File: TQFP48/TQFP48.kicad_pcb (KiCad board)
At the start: 2 copper layers, 61.2 x 18 mm, 11 parts, among them J1 Conn_01x24, J2 Conn_02x24_Counter_Clockwise, J3 Conn_02x24_Counter_Clockwise, J4 Conn_01x24, J5 Conn_01x05

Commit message: Board Updates
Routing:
- net Net-(J2-Pad48): track 54.5 -> 62.1 mm
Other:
- board size 61.2 x 18 mm -> 61 x 17.8 mm
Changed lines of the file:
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@@
     (thickness 1.6)
     (drawings 76)
-    (tracks 326)
+    (tracks 327)
     (zones 0)
     (modules 11)
@@
     (38 B.Mask user hide)
     (39 F.Mask user hide)
-    (40 Dwgs.User user)
+    (40 Dwgs.User user hide)
     (41 Cmts.User user hide)
     (42 Eco1.User user hide)
@@
       (xy 0.500964 -3.601424)) (layer F.SilkS) (width 0.01))
   )
-  (dimension 18.034 (width 0.15) (layer Dwgs.User)
-    (gr_text "18.034 mm" (at 30.196 35.56 270) (layer Dwgs.User)
+  (gr_line (start 97.917 43.18) (end 97.917 27.94) (layer Edge.Cuts) (width 0.05))
+  (gr_line (start 38.227 44.45) (end 96.647 44.45) (layer Edge.Cuts) (width 0.05))
+  (gr_line (start 36.957 27.94) (end 36.957 43.18) (layer Edge.Cuts) (width 0.05))
+  (gr_line (start 96.647 26.67) (end 38.227 26.67) (layer Edge.Cuts) (width 0.05))
+  (gr_arc (start 96.647 27.94) (end 97.917 27.94) (angle -90) (layer Edge.Cuts) (width 0.05))
+  (gr_arc (start 96.647 43.18) (end 96.647 44.45) (angle -90) (layer Edge.Cuts) (width 0.05))
+  (gr_arc (start 38.227 43.18) (end 36.957 43.18) (angle -90) (layer Edge.Cuts) (width 0.05))
+  (gr_arc (start 38.227 27.94) (end 38.227 26.67) (angle -90) (layer Edge.Cuts) (width 0.05))
+  (dimension 17.78 (width 0.15) (layer Dwgs.User)
+    (gr_text "17.780 mm" (at 30.323 35.56 270) (layer Dwgs.User)
       (effects (font (size 1 1) (thickness 0.15)) hide)
     )
-    (feature1 (pts (xy 38.227 44.577) (xy 30.909579 44.577)))
-    (feature2 (pts (xy 38.227 26.543) (xy 30.909579 26.543)))
-    (crossbar (pts (xy 31.496 26.543) (xy 31.496 44.577)))
-    (arrow1a (pts (xy 31.496 44.577) (xy 30.909579 43.450496)))
-    (arrow1b (pts (xy 31.496 44.577) (xy 32.082421 43.450496)))
-    (arrow2a (pts (xy 31.496 26.543) (xy 30.909579 27.669504)))
-    (arrow2b (pts (xy 31.496 26.543) (xy 32.082421 27.669504)))
+    (feature1 (pts (xy 38.354 44.45) (xy 31.036579 44.45)))
+    (feature2 (pts (xy 38.354 26.67) (xy 31.036579 26.67)))
+    (crossbar (pts (xy 31.623 26.67) (xy 31.623 44.45)))
+    (arrow1a (pts (xy 31.623 44.45) (xy 31.036579 43.323496)))
+    (arrow1b (pts (xy 31.623 44.45) (xy 32.209421 43.323496)))
+    (arrow2a (pts (xy 31.623 26.67) (xy 31.036579 27.796504)))
+    (arrow2b (pts (xy 31.623 26.67) (xy 32.209421 27.796504)))
   )
   (dimension 15.24 (width 0.15) (layer Dwgs.User)
@@
     (arrow2b (pts (xy 38.227 24.511) (xy 39.353504 23.924579)))
   )
-  (dimension 61.214 (width 0.15) (layer Dwgs.User)
-    (gr_text "61.214 mm" (at 67.437 20.798) (layer Dwgs.User)
+  (dimension 60.96 (width 0.15) (layer Dwgs.User)
+    (gr_text "60.960 mm" (at 67.437 20.798) (layer Dwgs.User)
       (effects (font (size 1 1) (thickness 0.15)) hide)
     )
-    (feature1 (pts (xy 98.044 27.94) (xy 98.044 21.511579)))
-    (feature2 (pts (xy 36.83 27.94) (xy 36.83 21.511579)))
-    (crossbar (pts (xy 36.83 22.098) (xy 98.044 22.098)))
-    (arrow1a (pts (xy 98.044 22.098) (xy 96.917496 22.684421)))
-    (arrow1b (pts (xy 98.044 22.098) (xy 96.917496 21.511579)))
-    (arrow2a (pts (xy 36.83 22.098) (xy 37.956504 22.684421)))
-    (arrow2b (pts (xy 36.83 22.098) (xy 37.956504 21.511579)))
+    (feature1 (pts (xy 97.917 27.94) (xy 97.917 21.511579)))
+    (feature2 (pts (xy 36.957 27.94) (xy 36.957 21.511579)))
+    (crossbar (pts (xy 36.957 22.098) (xy 97.917 22.098)))
+    (arrow1a (pts (xy 97.917 22.098) (xy 96.790496 22.684421)))
+    (arrow1b (pts (xy 97.917 22.098) (xy 96.790496 21.511579)))
+    (arrow2a (pts (xy 36.957 22.098) (xy 38.083504 22.684421)))
+    (arrow2b (pts (xy 36.957 22.098) (xy 38.083504 21.511579)))
   )
   (gr_text GND (at 40.894 30.48 180) (layer B.SilkS)
@@
     (effects (font (size 1 0.9) (thickness 0.15)))
   )
-  (gr_line (start 98.044 43.18) (end 98.044 27.94) (layer Edge.Cuts) (width 0.05))
-  (gr_line (start 38.227 44.577) (end 96.647 44.577) (layer Edge.Cuts) (width 0.05))
-  (gr_line (start 36.83 27.94) (end 36.83 43.18) (layer Edge.Cuts) (width 0.05))
-  (gr_line (start 96.647 26.543) (end 38.227 26.543) (layer Edge.Cuts) (width 0.05))
-  (gr_arc (start 96.647 27.94) (end 98.044 27.94) (angle -90) (layer Edge.Cuts) (width 0.05))
-  (gr_arc (start 96.647 43.18) (end 96.647 44.577) (angle -90) (layer Edge.Cuts) (width 0.05))
-  (gr_arc (start 38.227 43.18) (end 36.83 43.18) (angle -90) (layer Edge.Cuts) (width 0.05))
-  (gr_arc (start 38.227 27.94) (end 38.227 26.543) (angle -90) (layer Edge.Cuts) (width 0.05))
   (segment (start 72.324876 36.558788) (end 72.850088 37.084) (width 0.25) (layer F.Cu) (net 1))
   (segment (start 72.850088 37.084) (end 90.551 37.084) (width 0.25) (layer F.Cu) (net 1))
@@
   (segment (start 61.02373 32.258) (end 42.545 32.258) (width 0.127) (layer B.Cu) (net 25))
   (segment (start 42.545 32.258) (end 39.352848 29.065848) (width 0.127) (layer B.Cu) (net 25))
+  (segment (start 43.587955 33.300955) (end 38.227 27.94) (width 0.25) (layer F.Cu) (net 25))
   (segment (start 40.767 27.94) (end 46.355 33.528) (width 0.25) (layer F.Cu) (net 26))
   (segment (start 62.22302 33.528) (end 62.902678 34.207658) (width 0.25) (layer F.Cu) (net 26))
@@
     (polygon
       (pts
-        (xy 36.83 26.543) (xy 98.044 26.543) (xy 98.044 44.577) (xy 36.83 44.577)
+        (xy 36.957 26.67) (xy 97.917 26.67) (xy 97.917 44.45) (xy 36.957 44.45)
       )
     )
@@
     (polygon
       (pts
-        (xy 36.83 26.543) (xy 98.044 26.543) (xy 98.044 44.577) (xy 36.83 44.577)
+        (xy 36.957 26.67) (xy 97.917 26.67) (xy 97.917 44.45) (xy 36.957 44.45)
       )
     )

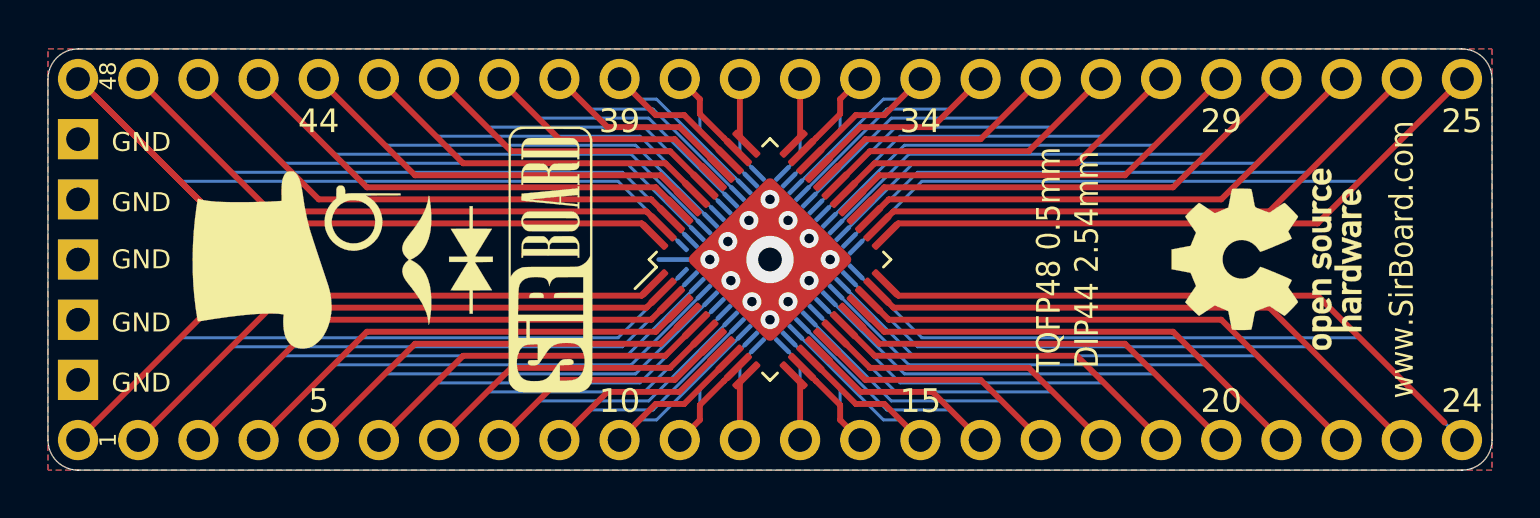
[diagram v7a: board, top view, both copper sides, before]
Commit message: Breakout Boards Revision 2
Renders updated, silkscreen text improved, blurry silkscreen items removed/resized.
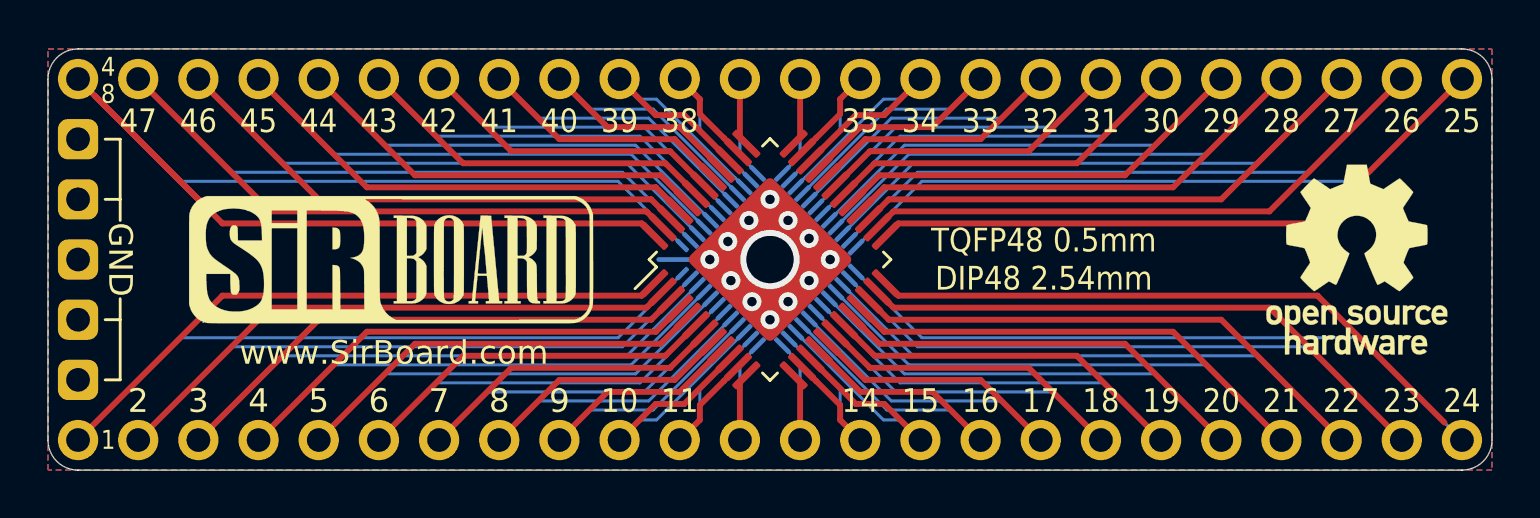
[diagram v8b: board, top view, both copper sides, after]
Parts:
- removed the G*** at (79.0, 35.6)
- removed the G*** at (88.4, 35.6)
- removed the G*** at (49.4, 35.6)
- removed the REF** at (50.8, 35.6)
- added G***: LOGO, logo:logo94x134, B.Cu at (44.6, 35.6)
- added G***: LOGO, logo:SirBoard171x54, B.Cu at (85.2, 35.6)
- G***: footprint logo:SirBoard112x35 -> logo:SirBoard171x54
- moved G*** 6.73 mm to (51.4, 35.6), turned to 0 degrees
- moved REF** 3.81 mm to (92.2, 35.6), turned to 0 degrees
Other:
- board text added: "11"
- board text added: "12"
- board text added: "13"
- board text added: "14"
- board text added: "16"
- board text added: "17"
- board text added: "18"
- board text added: "19"
- board text added: "2"
- board text added: "21"
- board text added: "22"
- board text added: "23"
- board text added: "26"
- board text added: "27"
- board text added: "28"
- board text added: "3"
- board text added: "30"
- board text added: "31"
- board text added: "32"
- board text added: "33"
- board text added: "35"
- board text added: "36"
- board text added: "37"
- board text added: "38"
- board text added: "4"
- board text added: "40"
- board text added: "41"
- board text added: "42"
- board text added: "43"
- board text added: "45"
- board text added: "46"
- board text added: "47"
- board text added: "5x5QFN48 0.4mm DIP44 2.54mm"
- board text added: "6"
- board text added: "7"
- board text added: "8"
- board text added: "9"
- board text added: "TQFP48 0.5mm DIP48 2.54mm"
- board text removed: "QFN48 0.4mm DIP44 2.54mm"
- board text removed: "TQFP48 0.5mm DIP44 2.54mm"
